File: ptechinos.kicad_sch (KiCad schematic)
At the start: 77 parts, among them J1 Trackball (Serial), J2 Battery, J3 Trackball JST (Serial), J4 TRRS, J5 Trackpad I2C, J6 OLED Header (I2C), J7 Pogo, J8 Trackball Header (Serial), SW1 SW_Power, SW2 Reset, SW3 Reset, U1 ProMicro

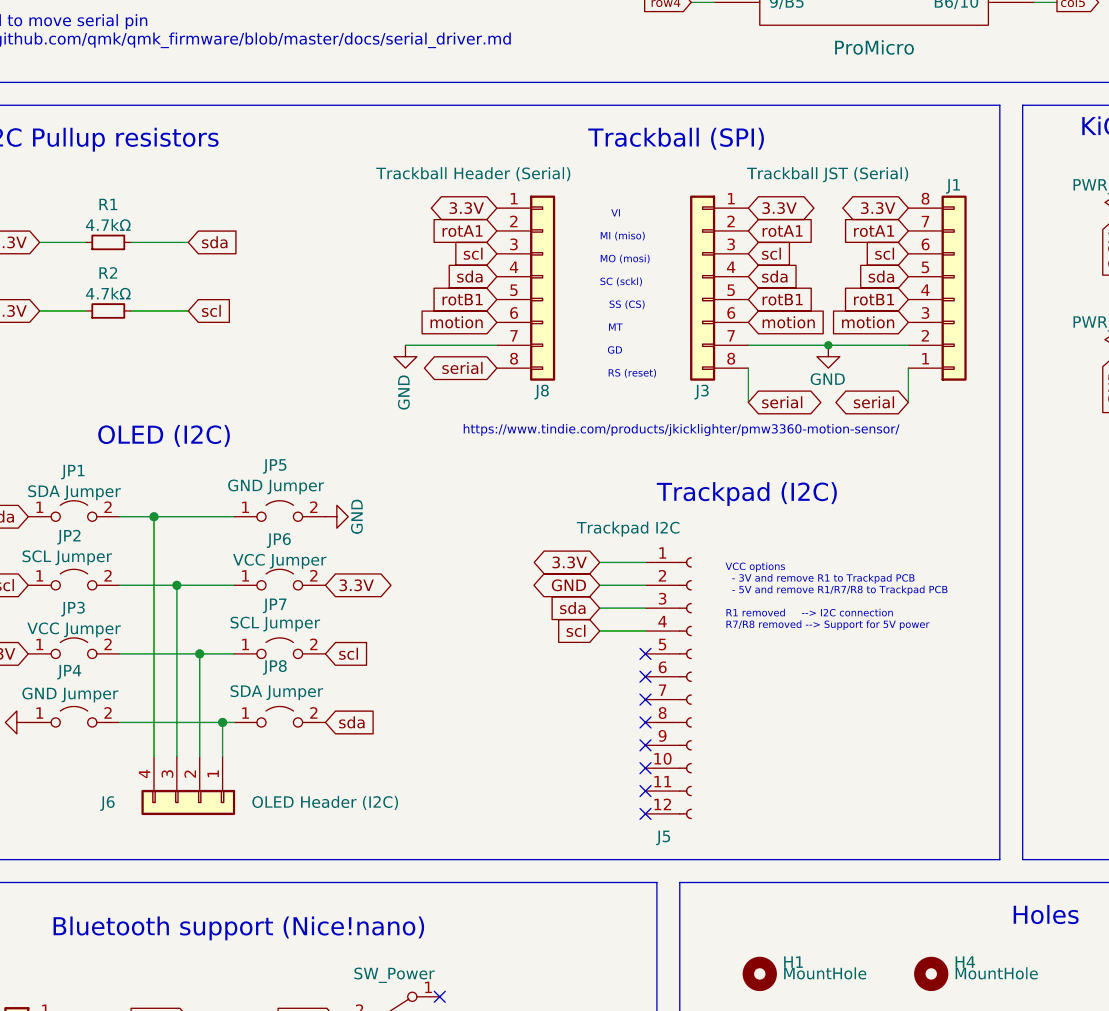
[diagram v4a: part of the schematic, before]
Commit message: 💄 - More succinct silkscreens for modules.
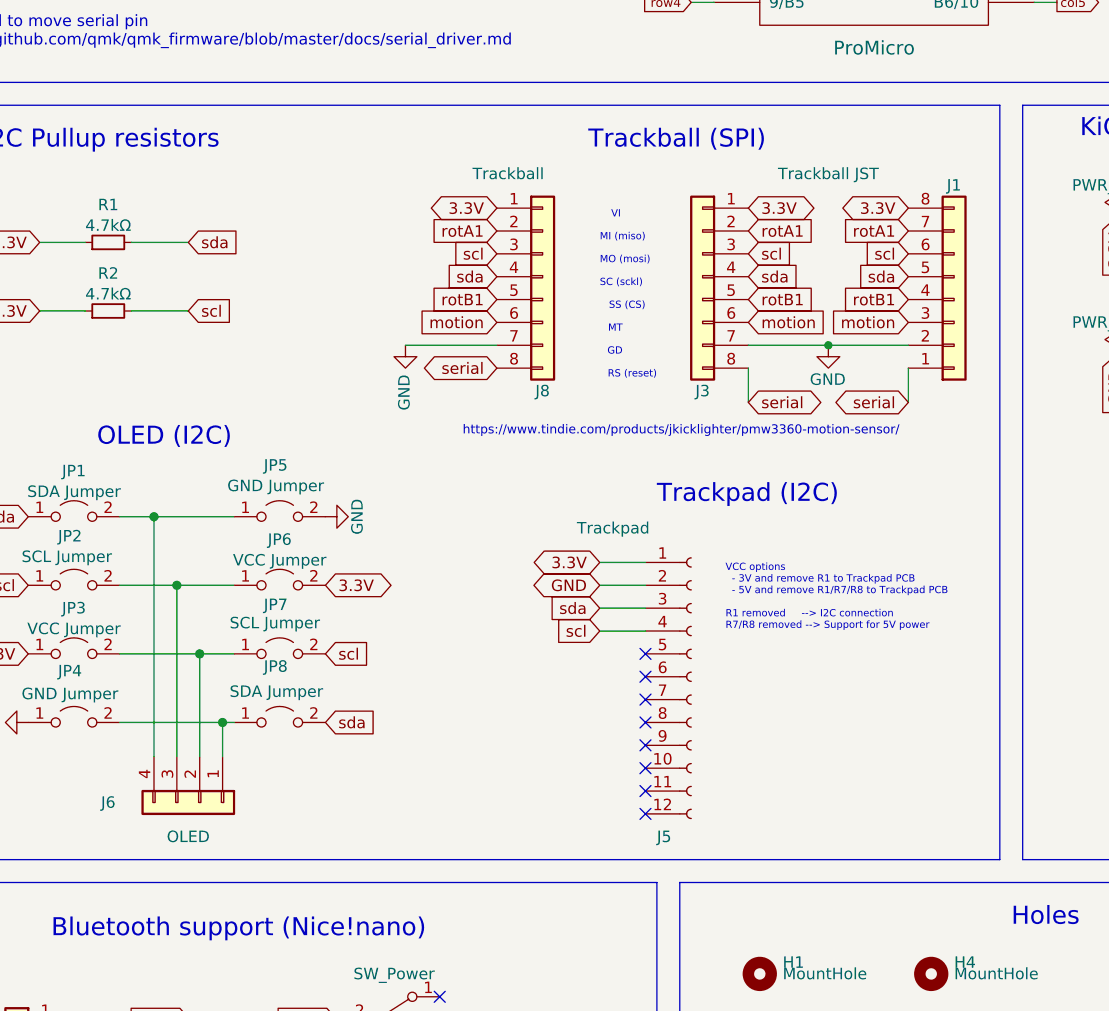
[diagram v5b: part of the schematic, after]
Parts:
- J3: value Trackball JST (Serial) -> Trackball JST
- J5: value Trackpad I2C -> Trackpad
- J6: value OLED Header (I2C) -> OLED
- J8: value Trackball Header (Serial) -> Trackball
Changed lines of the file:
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@@
   (title_block
     (title "Ptechinos")
-    (date "2022-10-23")
+    (date "2022-11-01")
     (rev "0.6")
     (comment 1 "A crossover between Pteron36 and Balbuzard.")
@@
       (effects (font (size 1.27 1.27)) (justify left))
     )
-    (property "Value" "Trackpad I2C" (id 1) (at 87.63 125.73 0)
+    (property "Value" "Trackpad" (id 1) (at 87.63 125.73 0)
       (effects (font (size 1.27 1.27)) (justify left))
     )
@@
     (in_bom yes) (on_board yes)
     (property "Reference" "J8" (id 0) (at 83.82 110.49 0))
-    (property "Value" "Trackball Header (Serial)" (id 1) (at 76.2 86.36 0))
+    (property "Value" "Trackball" (id 1) (at 80.01 86.36 0))
     (property "Footprint" "ptechinos:PMW3360" (id 2) (at 83.82 97.79 0)
       (effects (font (size 1.27 1.27)) hide)
@@
     (in_bom no) (on_board yes)
     (property "Reference" "J6" (id 0) (at 35.56 156.21 90))
-    (property "Value" "OLED Header (I2C)" (id 1) (at 59.69 156.21 90))
+    (property "Value" "OLED" (id 1) (at 44.45 160.02 90))
     (property "Footprint" "ptechinos:OLED" (id 2) (at 45.72 156.21 0)
       (effects (font (size 1.27 1.27)) hide)
@@
     (in_bom yes) (on_board yes)
     (property "Reference" "J3" (id 0) (at 101.6 110.49 0))
-    (property "Value" "Trackball JST (Serial)" (id 1) (at 115.57 86.36 0))
+    (property "Value" "Trackball JST" (id 1) (at 115.57 86.36 0))
     (property "Footprint" "Connector_JST:JST_SH_BM08B-SRSS-TB_1x08-1MP_P1.00mm_Vertical" (id 2) (at 101.6 97.79 0)
       (effects (font (size 1.27 1.27)) hide)
@@
     )
     (path "/f6399dd9-c1f4-4a0a-8f1e-6495630fc0ad"
-      (reference "J3") (unit 1) (value "Trackball JST (Serial)") (footprint "Connector_JST:JST_SH_BM08B-SRSS-TB_1x08-1MP_P1.00mm_Vertical")
+      (reference "J3") (unit 1) (value "Trackball JST") (footprint "Connector_JST:JST_SH_BM08B-SRSS-TB_1x08-1MP_P1.00mm_Vertical")
     )
     (path "/89410a4f-cc6a-4037-96a0-5a28865a1455"
@@
     )
     (path "/17efe087-3c06-4228-b0b9-f81dc95b2c2f"
-      (reference "J5") (unit 1) (value "Trackpad I2C") (footprint "ptechinos:GCT_FFC2B35-12-G_R")
+      (reference "J5") (unit 1) (value "Trackpad") (footprint "ptechinos:GCT_FFC2B35-12-G_R")
     )
     (path "/bcc3f068-dd7c-4997-80d9-41bb8616ad34"
-      (reference "J6") (unit 1) (value "OLED Header (I2C)") (footprint "ptechinos:OLED")
+      (reference "J6") (unit 1) (value "OLED") (footprint "ptechinos:OLED")
     )
     (path "/e2fea733-a4a4-4fad-a2fe-b335d49ded07"
@@
     )
     (path "/5187f2ae-558c-4228-a74a-6bc711a2463a"
-      (reference "J8") (unit 1) (value "Trackball Header (Serial)") (footprint "ptechinos:PMW3360")
+      (reference "J8") (unit 1) (value "Trackball") (footprint "ptechinos:PMW3360")
     )
     (path "/36785586-f5d0-48d2-b235-eb5df464c3a2"

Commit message: ♻️ - Add updated pogo footprints. Clean silkscreens.
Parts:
- J7: footprint ptechinos:PinHeader_1x04_P2.54mm_Vertical -> ptechinos:Pogo_1x04_P2.5mm
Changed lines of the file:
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@@
   (title_block
     (title "Ptechinos")
-    (date "2022-11-01")
+    (date "2022-11-12")
     (rev "0.6")
     (comment 1 "A crossover between Pteron36 and Balbuzard.")
@@
       (effects (font (size 1.27 1.27)) (justify left))
     )
-    (property "Footprint" "ptechinos:PinHeader_1x04_P2.54mm_Vertical" (id 2) (at 218.44 124.46 0)
+    (property "Footprint" "ptechinos:Pogo_1x04_P2.5mm" (id 2) (at 218.44 124.46 0)
       (effects (font (size 1.27 1.27)) hide)
     )
@@
     )
     (path "/e2fea733-a4a4-4fad-a2fe-b335d49ded07"
-      (reference "J7") (unit 1) (value "Pogo") (footprint "ptechinos:PinHeader_1x04_P2.54mm_Vertical")
+      (reference "J7") (unit 1) (value "Pogo") (footprint "ptechinos:Pogo_1x04_P2.5mm")
     )
     (path "/5187f2ae-558c-4228-a74a-6bc711a2463a"

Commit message: ✨ - Add 3D models to parts. If part is from a read only resource then 3D part is added directly on the PCB footprint copy.
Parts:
- U1: footprint ptechinos:ProMicro_v2 -> ptechinos:RP2040
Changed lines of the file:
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@@
   (title_block
     (title "Ptechinos")
-    (date "2022-11-12")
+    (date "2022-11-18")
     (rev "0.6")
     (comment 1 "A crossover between Pteron36 and Balbuzard.")
@@
       (effects (font (size 1.524 1.524)))
     )
-    (property "Footprint" "ptechinos:ProMicro_v2" (id 2) (at 123.19 80.01 0)
+    (property "Footprint" "ptechinos:RP2040" (id 2) (at 123.19 80.01 0)
       (effects (font (size 1.524 1.524)) hide)
     )
@@
     )
     (path "/d4bd6363-447e-4df0-8f7c-7fdbb7d5fd88"
-      (reference "U1") (unit 1) (value "ProMicro") (footprint "ptechinos:ProMicro_v2")
-    )
-  )
+      (reference "U1") (unit 1) (value "ProMicro") (footprint "ptechinos:RP2040")
+    )
+  )

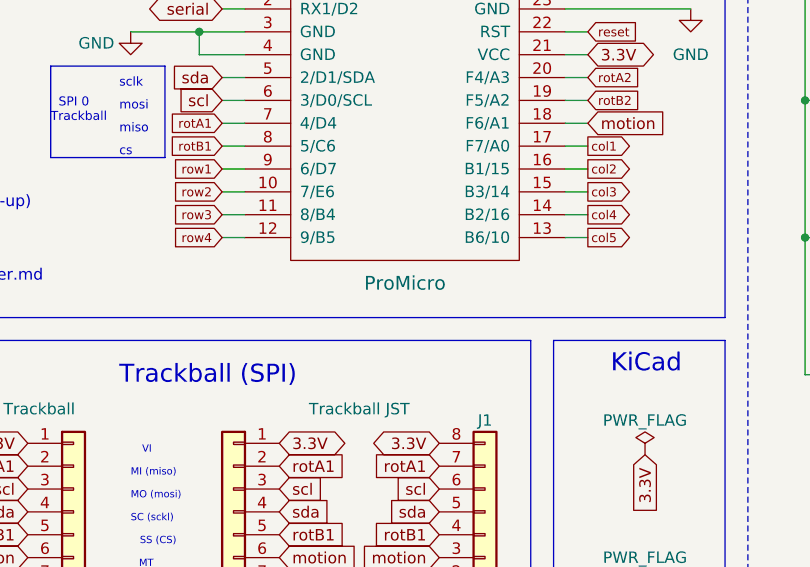
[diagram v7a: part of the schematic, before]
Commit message: ♻️ - Account for changes in 3D parts. Use SMD in place of Trough hole for diodes/capacitors/resistors.
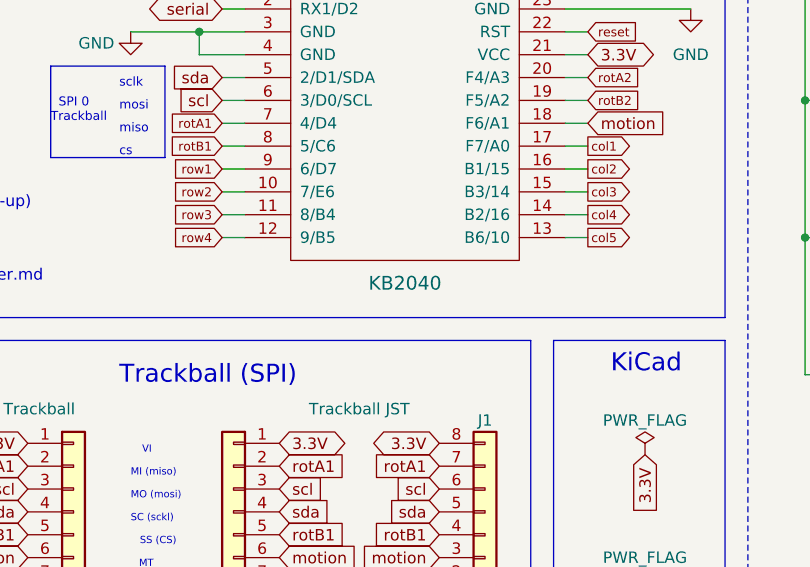
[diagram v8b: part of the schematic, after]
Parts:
- U1: value ProMicro -> KB2040; footprint ptechinos:RP2040 -> ptechinos:KB2040
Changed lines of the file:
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@@
   (title_block
     (title "Ptechinos")
-    (date "2022-11-18")
+    (date "2022-11-19")
     (rev "0.6")
     (comment 1 "A crossover between Pteron36 and Balbuzard.")
@@
       (effects (font (size 1.524 1.524)))
     )
-    (property "Value" "ProMicro" (id 1) (at 120.65 72.39 0)
+    (property "Value" "KB2040" (id 1) (at 120.65 72.39 0)
       (effects (font (size 1.524 1.524)))
     )
-    (property "Footprint" "ptechinos:RP2040" (id 2) (at 123.19 80.01 0)
+    (property "Footprint" "ptechinos:KB2040" (id 2) (at 123.19 80.01 0)
       (effects (font (size 1.524 1.524)) hide)
     )
@@
     )
     (path "/d4bd6363-447e-4df0-8f7c-7fdbb7d5fd88"
-      (reference "U1") (unit 1) (value "ProMicro") (footprint "ptechinos:RP2040")
-    )
-  )
+      (reference "U1") (unit 1) (value "KB2040") (footprint "ptechinos:KB2040")
+    )
+  )
